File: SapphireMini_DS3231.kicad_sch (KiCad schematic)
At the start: 8 parts, among them SW601 EVQP7C01P, U601 DS3231SN

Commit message: Corrected to get clean review on schematic
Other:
- title: Sapphire Mini -> Sapphire Mini M2
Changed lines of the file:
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@@
   (paper "USLetter")
   (title_block
-    (title "Sapphire Mini")
+    (title "Sapphire Mini M2")
+    (date "2022-09-26")
+    (rev "1")
     (company "Southern Methodist Univ")
+    (comment 1 "Chris Hayward")
   )
   (junction (at 137.16 59.69) (diameter 0) (color 0 0 0 0)

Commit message: Minor changes to annotation
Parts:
- R601, R602: value 4K75 -> 47; DPN 541-3984-1-ND -> 541-5440-1-ND; Digi-Key_PN 541-3984-1-ND -> 541-5440-1-ND; MPN CRCW06034K75FKEAC -> CRCW060347R0FKEAC; MacroFab_PN MF-RES-0603-4.7K -> MF-RES-0603-47
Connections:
- net I2C_SCL: now also R601.2; no longer R602.2, U601.16 (SCL)
- net I2C_SDA: now also R602.2; no longer R601.2, U601.15 (SDA)
- net P3V3: no longer R601.1, R602.1
- new net: R602.1, U601.15 (SDA)
- new net: R601.1, U601.16 (SCL)
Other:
- note added: "DS3231"
- note added: "I2C address: 0x68"

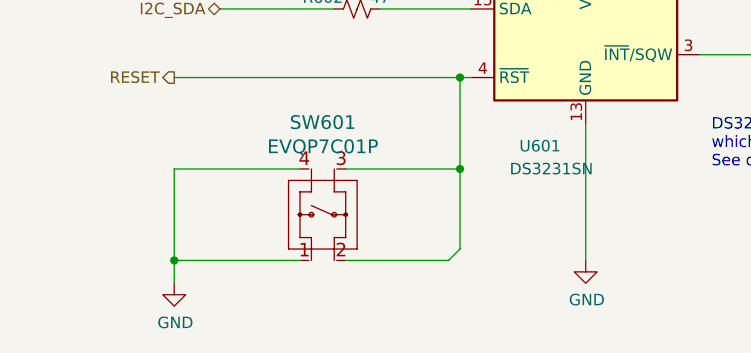
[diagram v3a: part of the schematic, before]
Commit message: Footprints complete. Starting layout
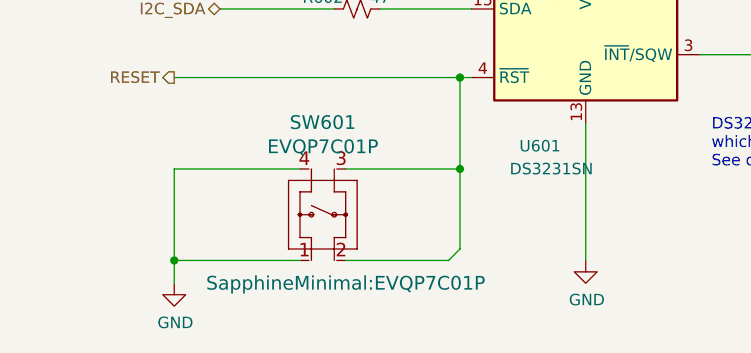
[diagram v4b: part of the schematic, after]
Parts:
- C601: MPN CL10B104KA8NNNC -> CL05A104KA5NNNC
- SW601: footprint EVQP7C/L_PAN -> SapphineMinimal:EVQP7C01P
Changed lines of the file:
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@@
       (effects (font (size 1.27 1.27)) hide)
     )
-    (property "Description" "1 µF ±10% 16V Ceramic Capacitor X7R 0805 " (id 15) (at 179.07 67.31 0)
+    (property "Description" "1 µF ±10% 16V Ceramic Capacitor X7R 0805 (2012 Metric)" (id 15) (at 179.07 67.31 0)
       (effects (font (size 1.27 1.27)) hide)
     )
@@
       (effects (font (size 1.27 1.27)) hide)
     )
-    (property "MPN" "CL10B104KA8NNNC" (id 5) (at 167.64 67.31 0)
+    (property "MPN" "CL05A104KA5NNNC" (id 5) (at 167.64 67.31 0)
       (effects (font (size 1.27 1.27)) hide)
     )
@@
       (effects (font (size 1.27 1.27)) hide)
     )
-    (property "Description" "0.1 µF ±10% 25V Ceramic Capacitor X7R 0603 (1608 Metric)" (id 15) (at 167.64 67.31 0)
+    (property "Description" "0.1 µF ±10% 25V Ceramic Capacitor X5R 0402 (1005 Metric)" (id 15) (at 167.64 67.31 0)
       (effects (font (size 1.27 1.27)) hide)
     )
@@
       (effects (font (size 1.524 1.524)))
     )
-    (property "Footprint" "EVQP7C/L_PAN" (id 2) (at 97.79 104.14 0)
-      (effects (font (size 1.524 1.524)) hide)
+    (property "Footprint" "SapphineMinimal:EVQP7C01P" (id 2) (at 113.03 111.76 0)
+      (effects (font (size 1.524 1.524)))
     )
     (property "Datasheet" "" (id 3) (at 83.82 105.41 0)

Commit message: Checkpoint
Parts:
- SW601: footprint SapphineMinimal:EVQP7C01P -> Sapphire:EVQP7C01P
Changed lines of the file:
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@@
       (effects (font (size 1.524 1.524)))
     )
-    (property "Footprint" "SapphineMinimal:EVQP7C01P" (id 2) (at 113.03 111.76 0)
+    (property "Footprint" "Sapphire:EVQP7C01P" (id 2) (at 113.03 111.76 0)
       (effects (font (size 1.524 1.524)))
     )

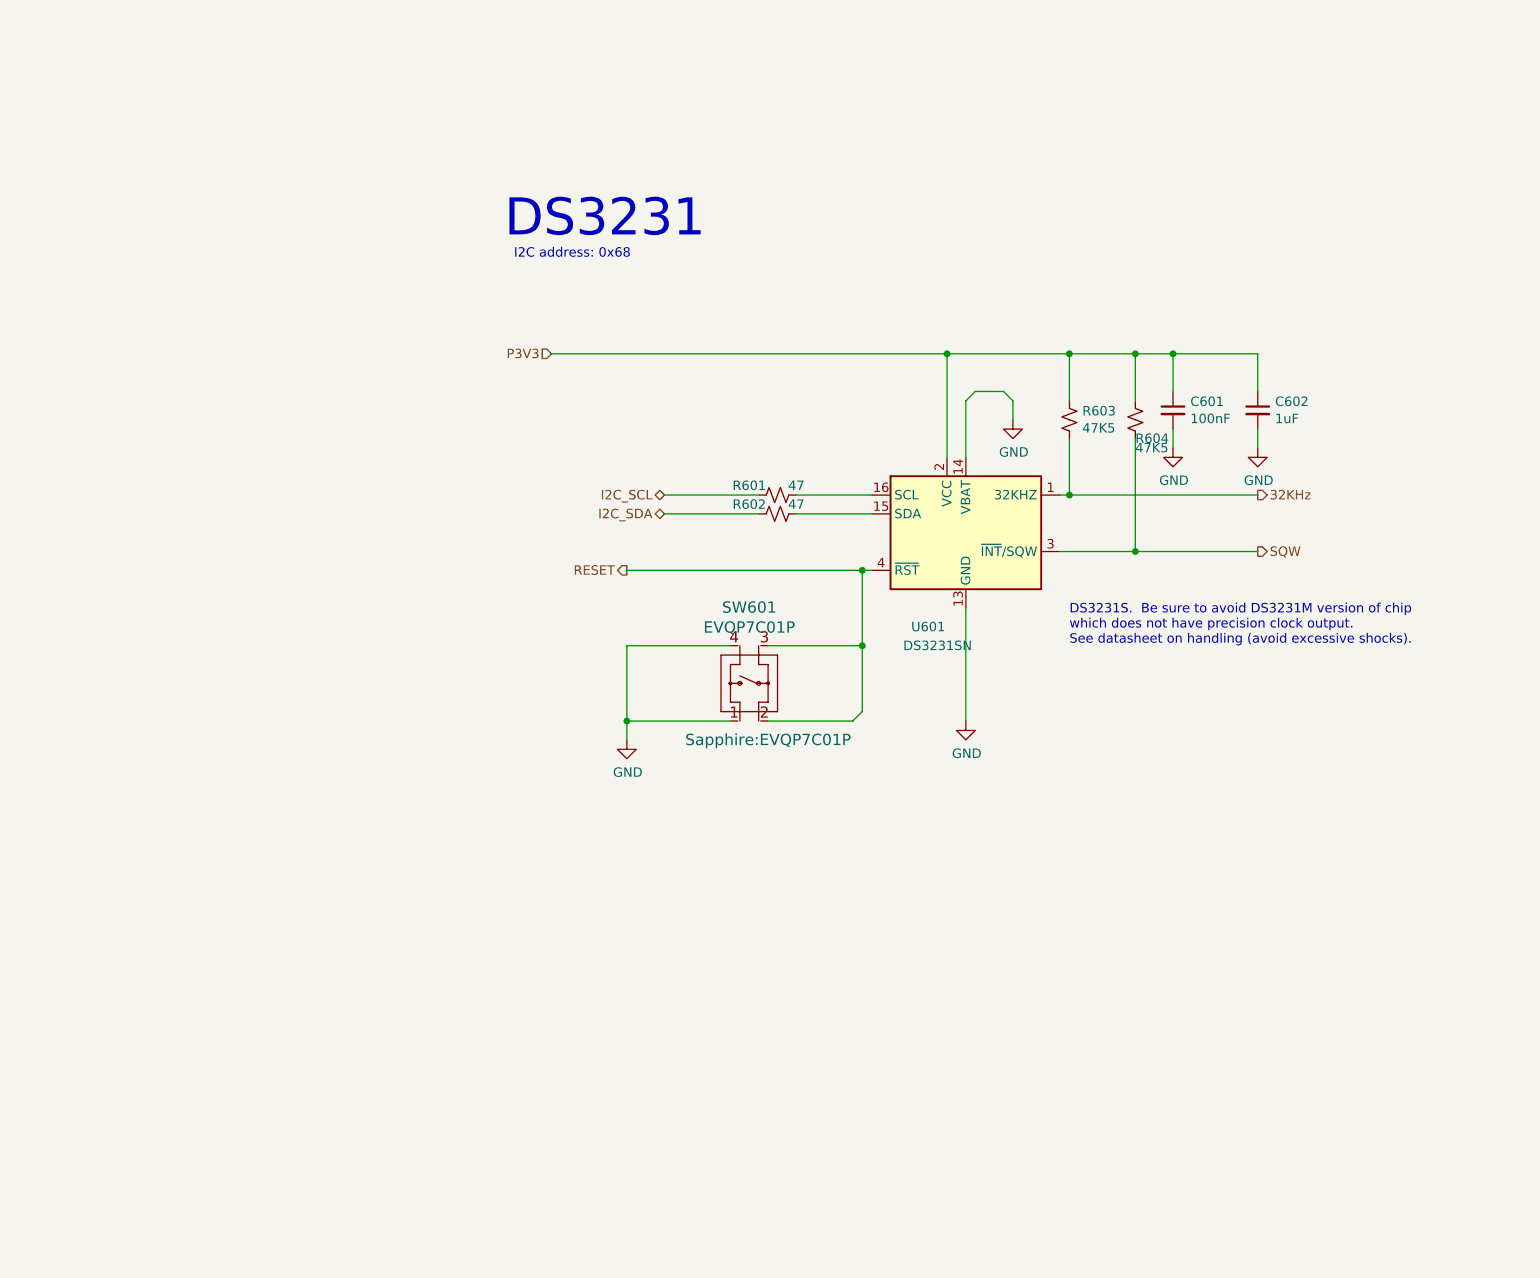
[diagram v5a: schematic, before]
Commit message: Clean PCB but Added new clock to schematic
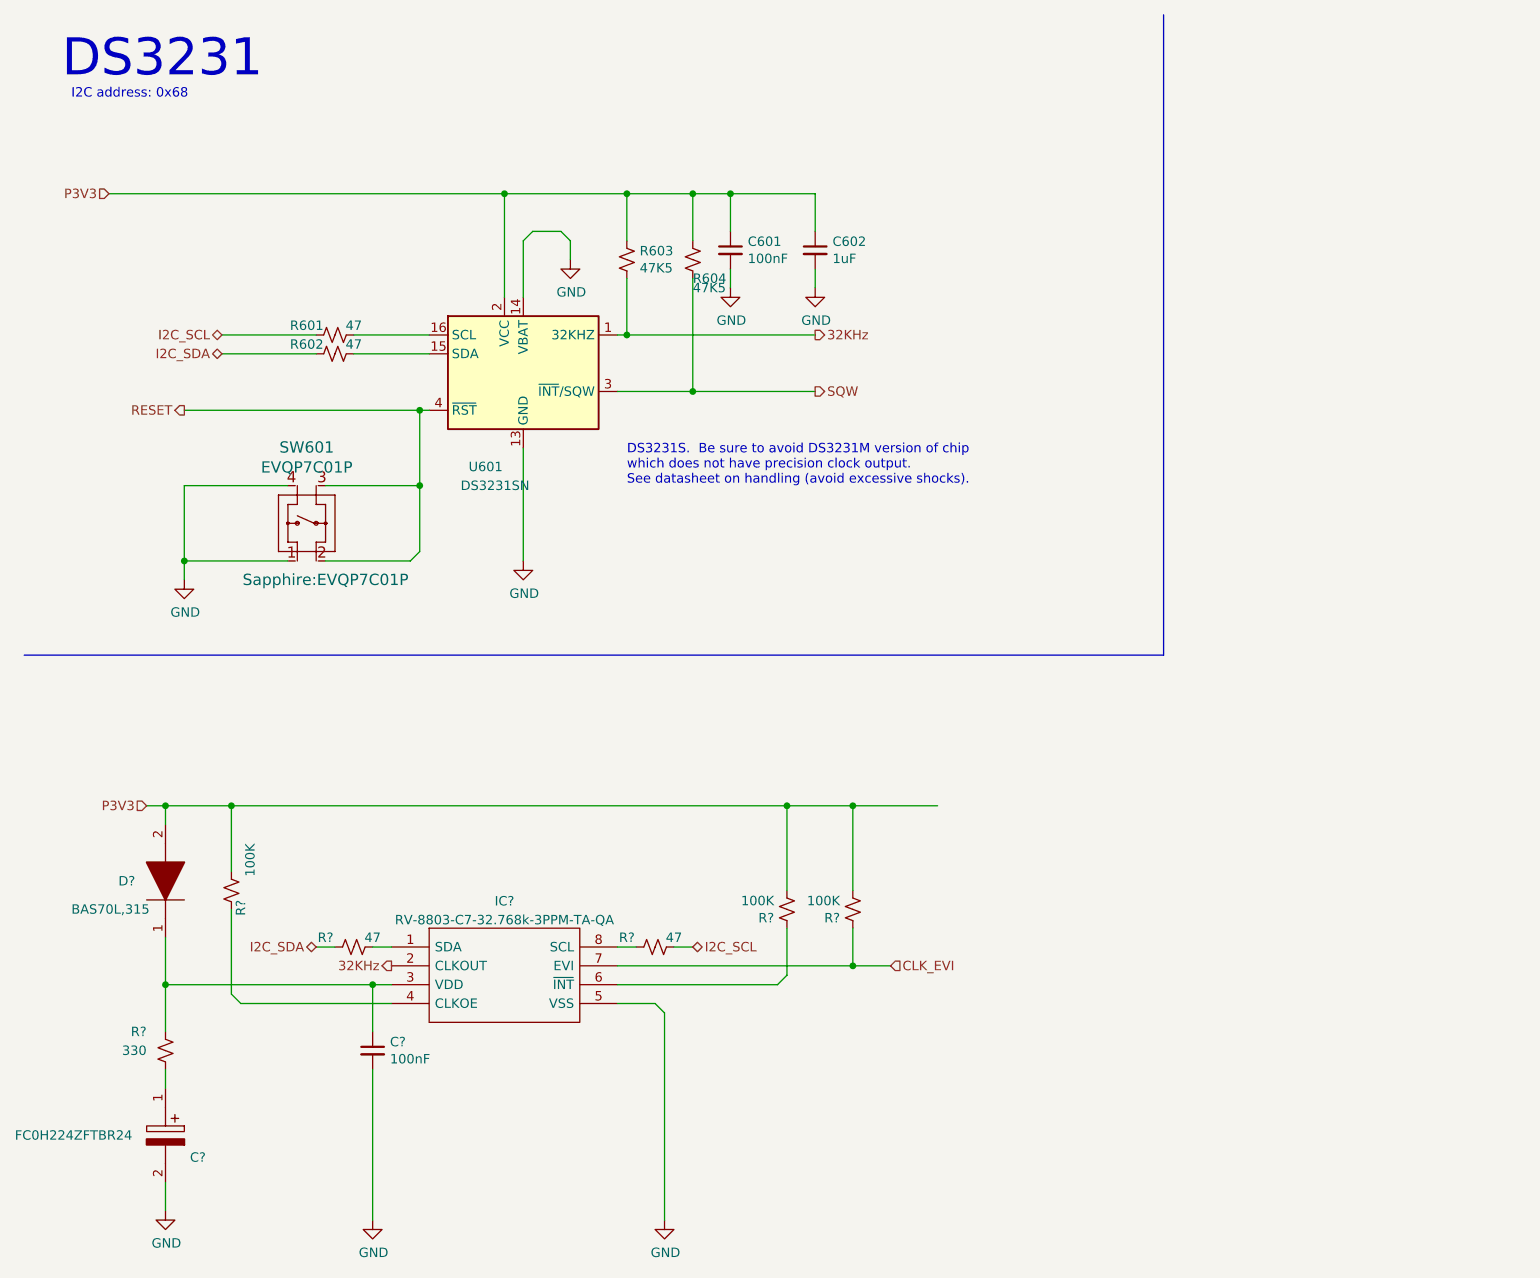
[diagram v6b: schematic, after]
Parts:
- added C?: 100nF, Capacitor_SMD:C_0603_1608Metric, symbol Device:C_Small
- added C?: FC0H224ZFTBR24, CAPAE1080X880N, symbol SamacSys_Parts:FC0H224ZFTBR24
- added D?: BAS70L,315, PESD5V0S1BL315, symbol SamacSys_Parts:BAS70L,315
- added IC?: RV-8803-C7-32.768k-3PPM-TA-QA, RV8803C7, symbol SamacSys_Parts:RV-8803-C7-32.768k-3PPM-TA-QA
- added R?: 330, Resistor_SMD:R_0603_1608Metric, symbol Device:R_Small_US
- added R? (x3): 100K, Resistor_SMD:R_0603_1608Metric, symbol Device:R_Small_US
- added R? (x2): 47, Resistor_SMD:R_0603_1608Metric, symbol Device:R_Small_US
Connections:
- net 32KHz: now also IC?.2 (CLKOUT)
- net GND: now also C?.2, C?.2, IC?.5 (VSS)
- net I2C_SCL: now also R?.1
- net I2C_SDA: now also R?.2
- net P3V3: now also D?.2, R?.2, R?.2, R?.2
- new net: IC?.1 (SDA), R?.1
- new net: C?.1, D?.1, IC?.3 (VDD), R?.2
- new net: IC?.4 (CLKOE), R?.1
- new net: IC?.6 (~{INT}), R?.1
- new net: IC?.8 (SCL), R?.2
- new net: C?.1, R?.1
- new net CLK_EVI: IC?.7 (EVI), R?.1
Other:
- moved on the sheet: C601, C602, R601, R602, R603, R604, SW601, U601

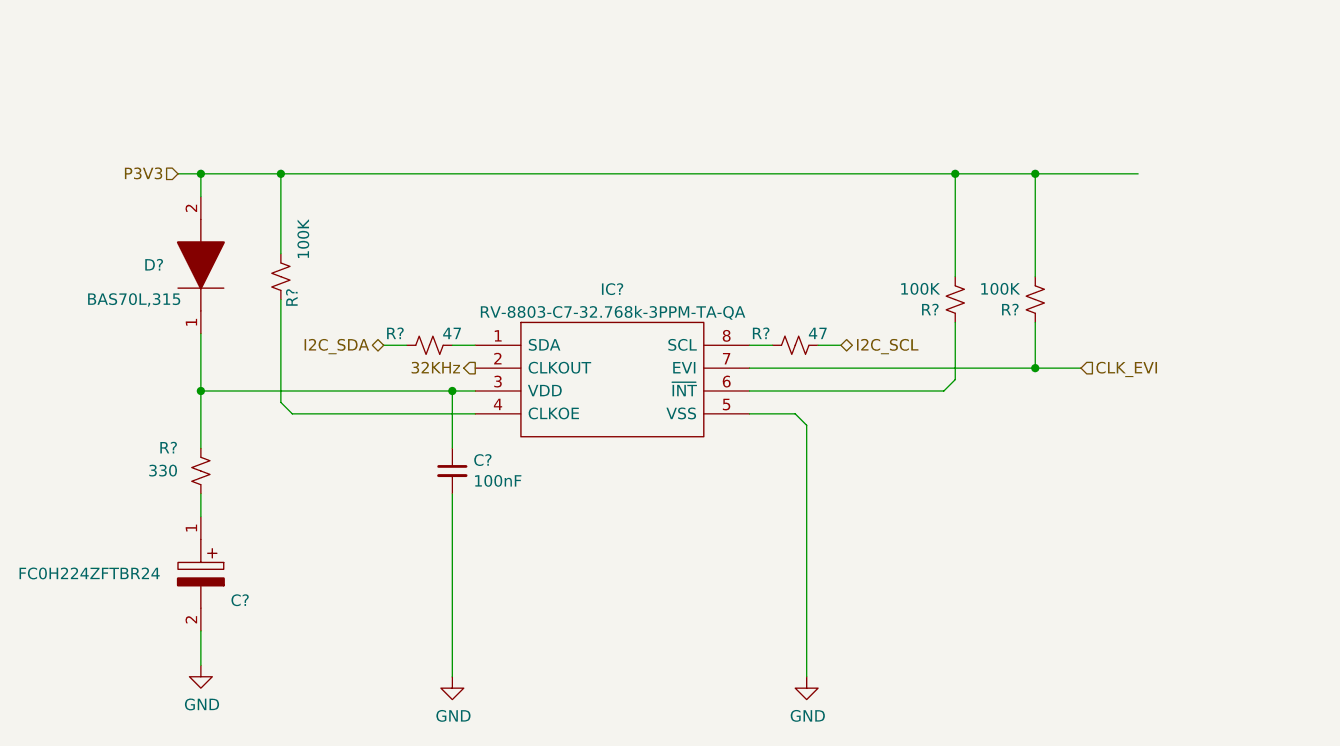
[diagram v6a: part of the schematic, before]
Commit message: Updating for parts avail
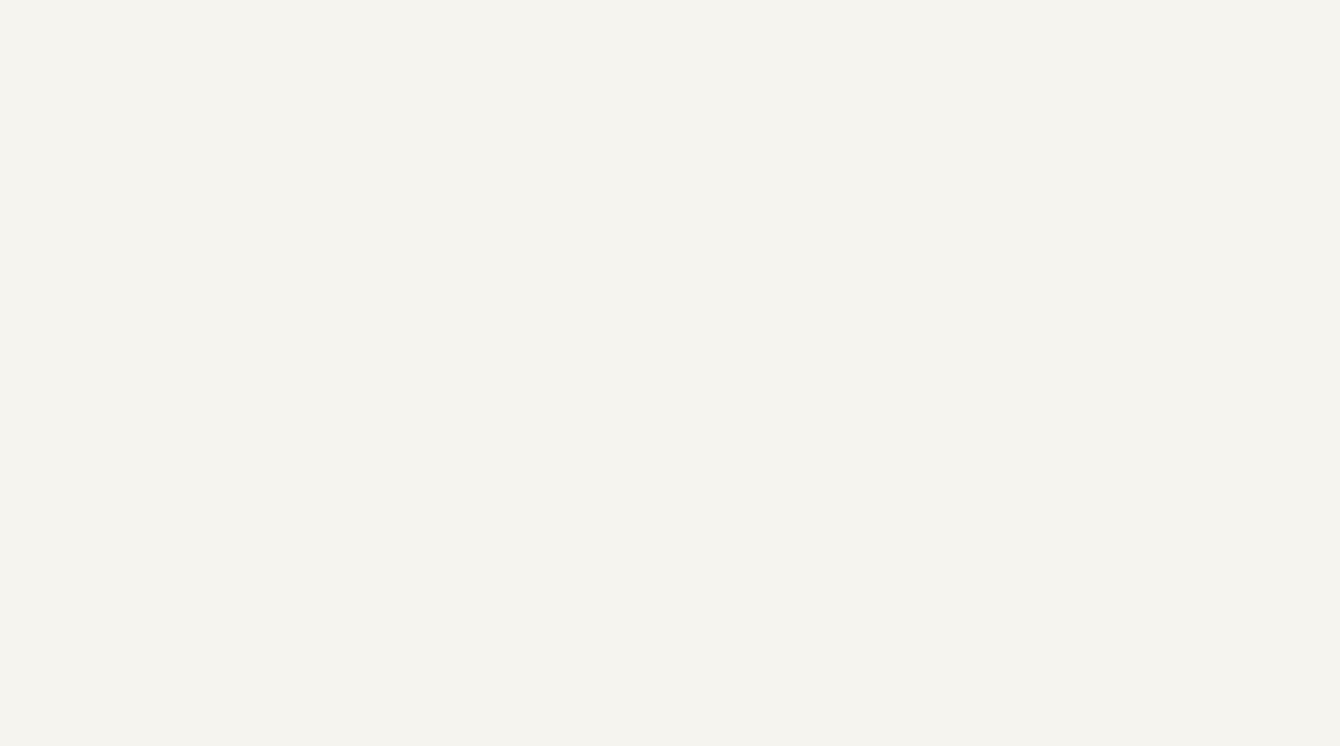
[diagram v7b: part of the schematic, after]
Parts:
- removed C?: 100nF, Capacitor_SMD:C_0603_1608Metric, symbol Device:C_Small
- removed C?: FC0H224ZFTBR24, CAPAE1080X880N, symbol SamacSys_Parts:FC0H224ZFTBR24
- removed D?: BAS70L,315, PESD5V0S1BL315, symbol SamacSys_Parts:BAS70L,315
- removed IC?: RV-8803-C7-32.768k-3PPM-TA-QA, RV8803C7, symbol SamacSys_Parts:RV-8803-C7-32.768k-3PPM-TA-QA
- removed R?: 330, Resistor_SMD:R_0603_1608Metric, symbol Device:R_Small_US
- removed R? (x3): 100K, Resistor_SMD:R_0603_1608Metric, symbol Device:R_Small_US
- removed R? (x2): 47, Resistor_SMD:R_0603_1608Metric, symbol Device:R_Small_US
